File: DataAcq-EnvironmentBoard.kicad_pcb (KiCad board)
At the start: 2 copper layers, 53 x 59 mm, 26 parts, among them J2 CAN Output, J3 CAN Input, J6 Breakout Connector, U4 Daughterboard Connector

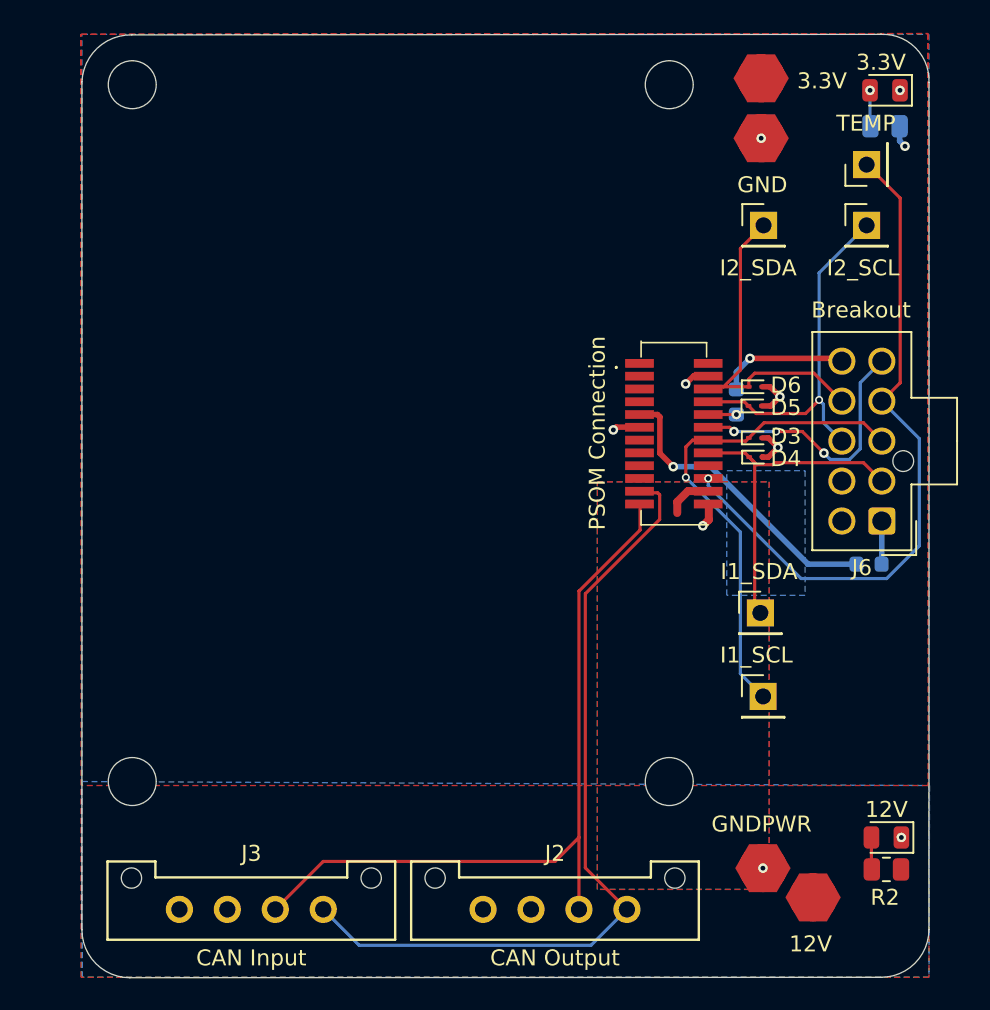
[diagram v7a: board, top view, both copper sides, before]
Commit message: traces for connector change
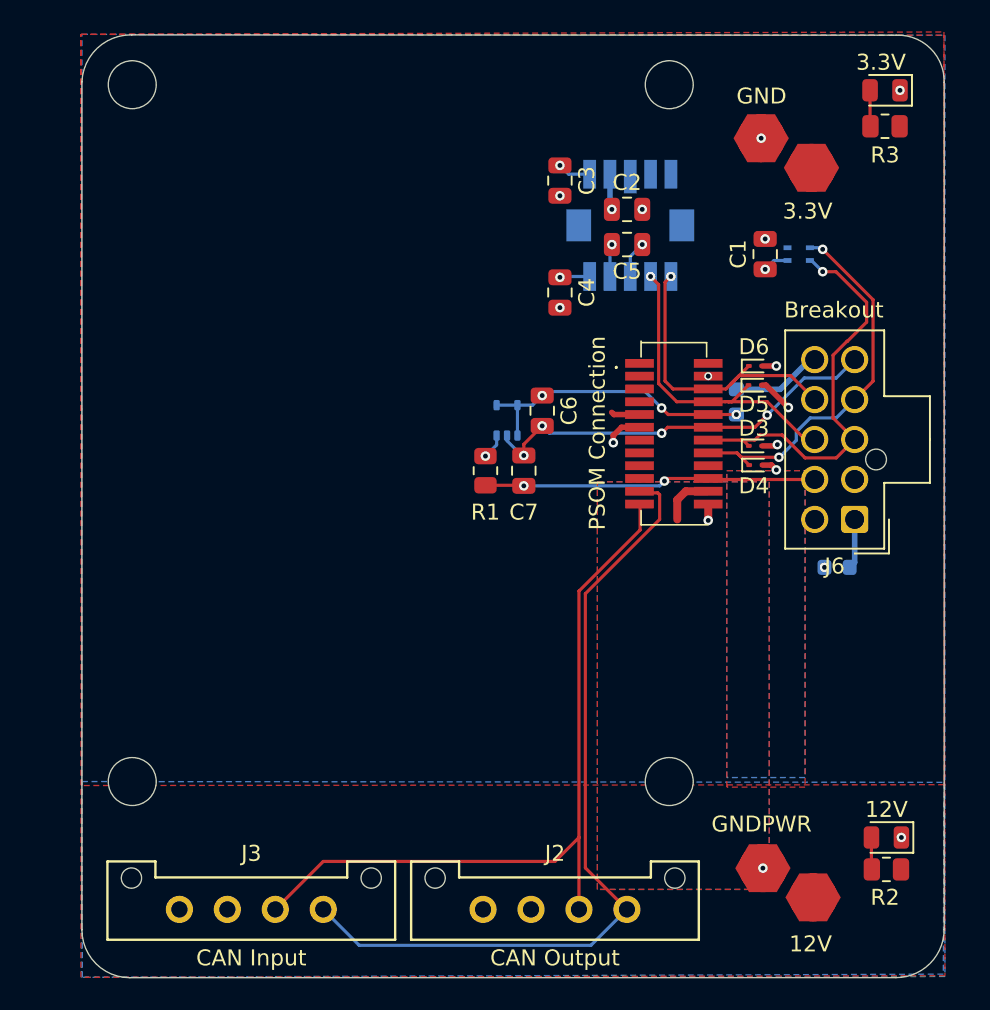
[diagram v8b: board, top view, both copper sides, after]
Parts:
- removed TP3, TP6, TP7, TP8, TP9: TestPoint, Connector_PinHeader_2.54mm:PinHeader_1x01_P2.54mm_Vertical
- added C1: 0.1uF, Capacitor_SMD:C_0805_2012Metric, F.Cu at (185.5, 85.0)
- added C2: 0.1uF, Capacitor_SMD:C_0805_2012Metric, F.Cu at (176.9, 82.2)
- added C3: 0.1uF, Capacitor_SMD:C_0805_2012Metric, F.Cu at (172.7, 80.4)
- added C4: 1uF, Capacitor_SMD:C_0805_2012Metric, F.Cu at (172.7, 87.4)
- added C5: 0.1uF, Capacitor_SMD:C_0805_2012Metric, F.Cu at (176.9, 84.4)
- added C6: 0.1uF, Capacitor_SMD:C_0805_2012Metric, F.Cu at (171.6, 94.8)
- added C7: 1uF, Capacitor_SMD:C_0805_2012Metric, F.Cu at (170.4, 98.5)
- added LOGO1: Arrow, images:arrow, B.Cu at (169.1, 86.2)
- added R1: 1k, Resistor_SMD:R_0805_2012Metric, F.Cu at (168.0, 98.5)
- added U1: SHT45, Sensor_Humidity:Sensirion_DFN-4_1.5x1.5mm_P0.8mm_SHT4x_NoCentralPad, B.Cu at (187.6, 85.0)
- added U2: FS3000-1005, SamacSys_Parts:FS30001005, B.Cu at (177.1, 83.2)
- added U3: LMT87DCK, Package_TO_SOT_SMD:SOT-353_SC-70-5, B.Cu at (169.3, 95.4)
- R3: moved to F.Cu
- moved LOGO4 12.8 mm to (167.8, 110.3)
- moved LOGO2 12.3 mm to (154.7, 110.1)
- moved TP4 6.43 mm to (188.4, 79.6)
- moved LOGO3 5.29 mm to (155.9, 91.4)
- moved F1 2.01 mm to (190.0, 104.6)
- moved J6 1.70 mm to (191.1, 101.6)
- moved D5 1.30 mm to (184.9, 93.2)
- moved D6 1.30 mm to (184.9, 92.0)
- moved D3 0.50 mm to (184.9, 97.0)
- moved D4 0.50 mm to (184.9, 98.2)
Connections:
- J6 pad 2: /I2C1_SDA -> unconnected-(J6-Pin_2-Pad2)
- J6 pad 4: /PA1(ADC) -> /I2C1_SDA
- J6 pad 7: unconnected-(J6-Pin_7-Pad7) -> /PA1(ADC)
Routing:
- net /PA1(ADC): track 43.1 -> 20.8 mm, vias 1 -> 2
- net VDDA: track 1.76 -> 17.8 mm, vias 1 -> 3
- net +3.3V: track 20.2 -> 5.67 mm, vias 2 -> 3
- net GNDA: track 16.7 -> 25.7 mm, vias 3 -> 4
- net /I2C1_SCL: track 31.0 -> 25.7 mm
- net /I2C2_SCL: track 22.9 -> 19.8 mm
- net /I2C1_SDA: track 21.7 -> 24.2 mm, vias 0 -> 2
- net /VDDA-out: track 8.11 -> 5.67 mm, vias 1 -> 0
- net /AFLW_TP1: track 0.00 -> 2.31 mm, vias 0 -> 1
- net /AFLW_VREG: track 0.00 -> 2.09 mm, vias 0 -> 1
- net /AFLW_TP2: track 0.00 -> 2.05 mm, vias 0 -> 1
- net /AFLW_VCM: track 0.00 -> 1.88 mm, vias 0 -> 1
- net /I2C2_SDA: track 20.9 -> 19.2 mm, vias 0 -> 1
- net /TEMP_OUT: track 0.00 -> 1.58 mm, vias 0 -> 1
- net GND: track 8.60 -> 7.37 mm, vias 6 -> 12
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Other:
- board size 53 x 59 mm -> 53.9 x 59 mm
- board text added: "Airflow"
- board text added: "Humidity"
- board text added: "Temp"
- board text removed: "I1_SCL"
- board text removed: "I1_SDA"
- board text removed: "I2_SCL"
- board text removed: "I2_SDA"
- board text removed: "TEMP"
